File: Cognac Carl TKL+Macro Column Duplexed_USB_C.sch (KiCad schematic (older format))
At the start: 202 parts, among them SW1 SW_Push, U1 ATmega32U4-AU, Y1 16MHz

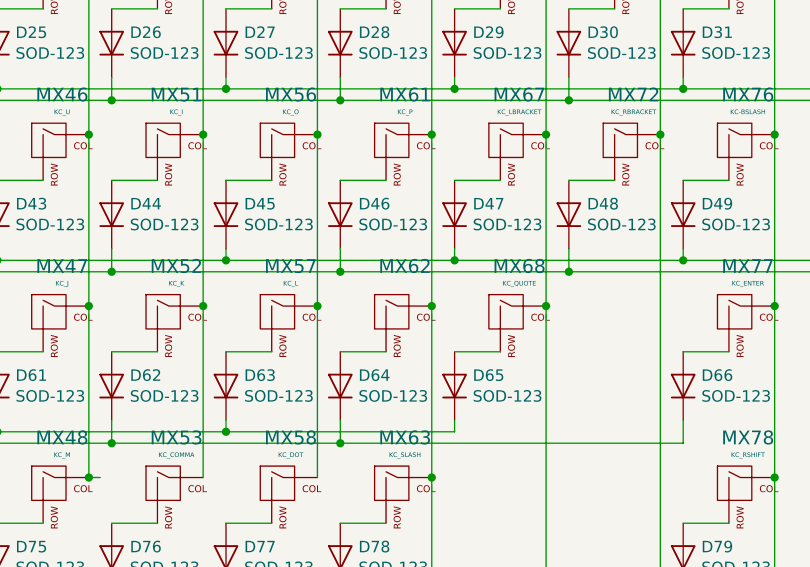
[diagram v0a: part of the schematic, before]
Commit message: Ran column traces, debating on whether to have columns on front or back of pcb
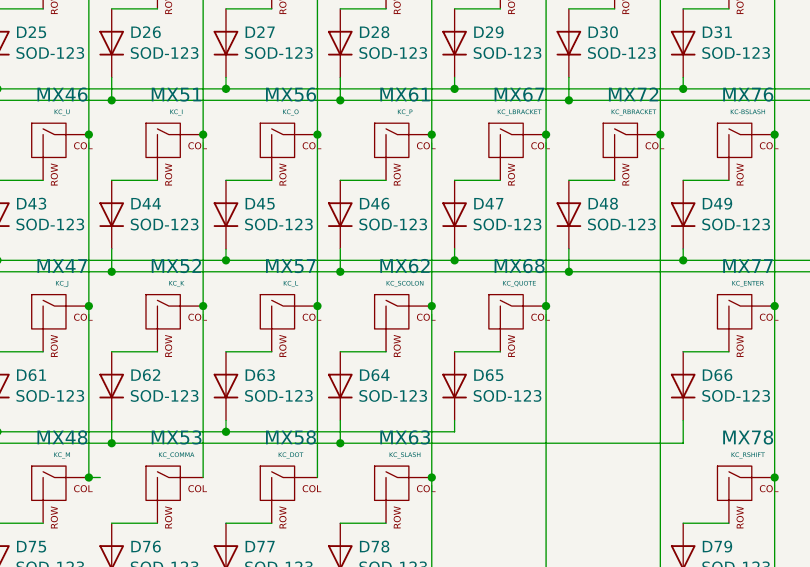
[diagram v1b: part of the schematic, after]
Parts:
- MX62: value (none) -> KC_SCOLON
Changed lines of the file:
@@
 P 7850 4050
 F 0 "MX62" H 7883 4273 60  0000 C CNN
-F 1 "KC_SCOLON
-" H 7883 4199 20  0000 C CNN
+F 1 "KC_SCOLON" H 7883 4199 20  0000 C CNN
 F 2 "MX_Only:MXOnly-1U-Hotswap" H 7225 4025 60  0001 C CNN
 F 3 "" H 7225 4025 60  0001 C CNN

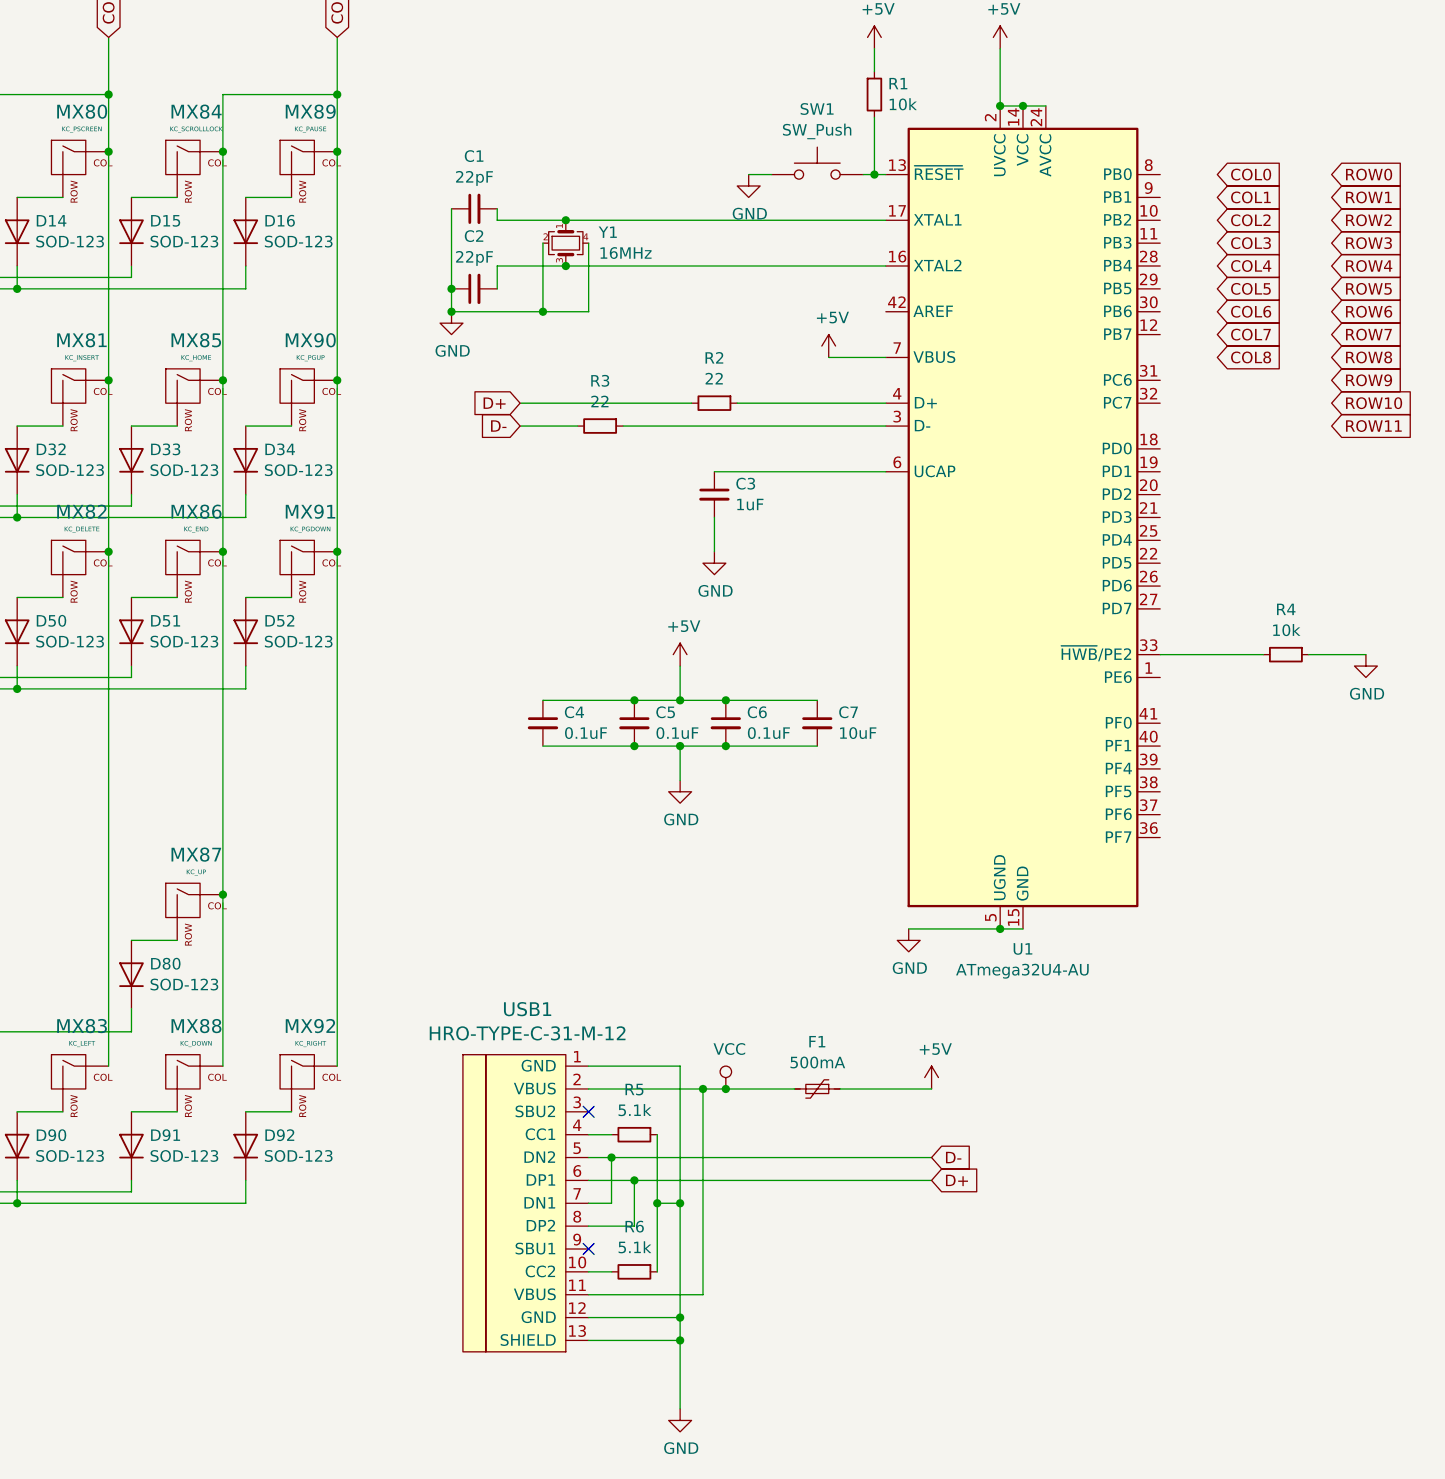
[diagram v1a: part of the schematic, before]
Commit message: completed routing, removed hotswap, added esd protection
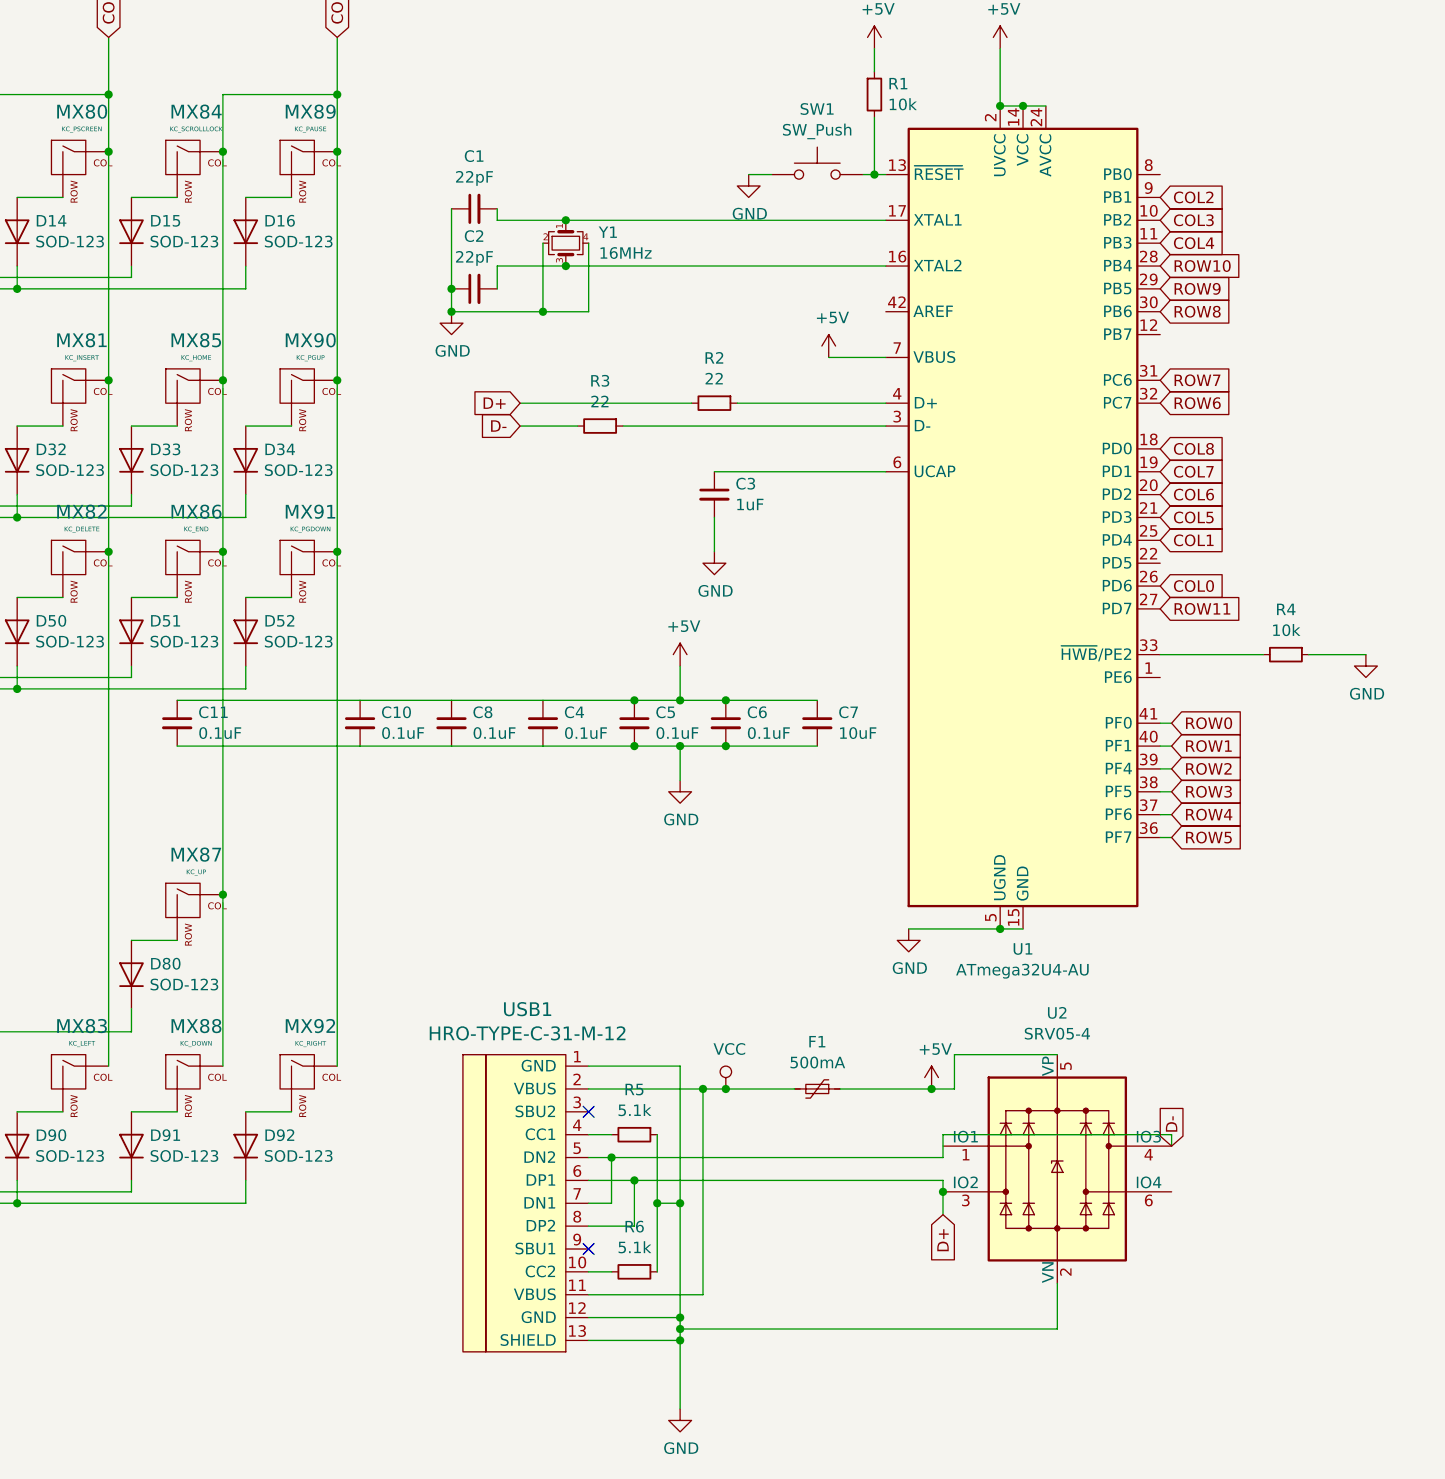
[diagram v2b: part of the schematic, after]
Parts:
- added C10, C11, C8: 0.1uF, Capacitor_SMD:C_0805_2012Metric, symbol Device:C_Small
- added U2: SRV05-4, Package_TO_SOT_SMD:SOT-23-6, symbol Power_Protection:SRV05-4
- MX1, MX12, MX13, MX14, MX15, MX17, MX18, MX19, MX2, MX20, MX21, MX23, MX24, MX25, MX26, MX27, MX28, MX29, MX3, MX30, MX31, MX32, MX33, MX34, MX35, MX36, MX37, MX38, MX39, MX4, MX40, MX41, MX42, MX44, MX45, MX46, MX47, MX48, MX49, MX5, MX50, MX51, MX52, MX53, MX54, MX55, MX56, MX57, MX58, MX59, MX6, MX60, MX61, MX62, MX63, MX65, MX66, MX67, MX68, MX7, MX70, MX71, MX72, MX74, MX80, MX81, MX82, MX83, MX84, MX85, MX86, MX87, MX88, MX89, MX90, MX91, MX92: footprint MX_Only:MXOnly-1U-Hotswap -> MX_Only:MXOnly-1U-NoLED
- MX10, MX77: footprint MX_Only:MXOnly-2.25U-Hotswap -> MX_Only:MXOnly-2.25U-NoLED
- MX11, MX16, MX22, MX64, MX69, MX73, MX79: footprint MX_Only:MXOnly-1.25U-Hotswap -> MX_Only:MXOnly-1.25U-NoLED
- MX43: footprint MX_Only:MXOnly-6.25U-Hotswap-ReversedStabilizers -> MX_Only:MXOnly-6.25U-ReversedStabilizers-NoLED
- MX75: footprint MX_Only:MXOnly-2U-Hotswap -> MX_Only:MXOnly-2U-NoLED
- MX76, MX8: footprint MX_Only:MXOnly-1.5U-Hotswap -> MX_Only:MXOnly-1.5U-NoLED
- MX78: footprint MX_Only:MXOnly-2.75U-Hotswap -> MX_Only:MXOnly-2.75U-NoLED
- MX9: footprint MX_Only:MXOnly-1.75U-Hotswap -> MX_Only:MXOnly-1.75U-NoLED
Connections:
- net +5V: now also C10.1, C11.1, C8.1, U2.5 (VP)
- net COL0: now also U1.26 (PD6)
- net COL1: now also U1.25 (PD4)
- net COL2: now also U1.9 (PB1)
- net COL3: now also U1.10 (PB2)
- net COL4: now also U1.11 (PB3)
- net COL5: now also U1.21 (PD3)
- net COL6: now also U1.20 (PD2)
- net COL7: now also U1.19 (PD1)
- net COL8: now also U1.18 (PD0)
- net D+: now also U2.3 (IO2)
- net D-: now also U2.4 (IO3)
- net GND: now also C10.2, C11.2, C8.2, U2.2 (VN)
- net ROW0: now also U1.41 (PF0)
- net ROW1: now also U1.40 (PF1)
- net ROW10: now also U1.28 (PB4)
- net ROW11: now also U1.27 (PD7)
- net ROW2: now also U1.39 (PF4)
- net ROW3: now also U1.38 (PF5)
- net ROW4: now also U1.37 (PF6)
- net ROW5: now also U1.36 (PF7)
- net ROW6: now also U1.32 (PC7)
- net ROW7: now also U1.31 (PC6)
- net ROW8: now also U1.30 (PB6)
- net ROW9: now also U1.29 (PB5)

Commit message: replaced crytsal with a murata oscillator. tidied up routing, and added filled zones.
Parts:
- removed C1, C2: 22pF, Capacitor_SMD:C_0805_2012Metric, symbol Device:C_Small
- removed Y1: 16MHz, Crystal:Crystal_SMD_3225-4Pin_3.2x2.5mm, symbol Device:Crystal_GND24_Small
- added D93, D94, D95: LED, LED_SMD:LED_0805_2012Metric, symbol Device:LED
- added R7, R8, R9: R_Small, Resistor_SMD:R_0805_2012Metric, symbol Device:R_Small
- added Y1: 16MHz, Crystal:Resonator_SMD_muRata_CSTxExxV-3Pin_3.0x1.1mm, symbol Device:Crystal_GND2_Small
- MX77: footprint MX_Only:MXOnly-2.25U-NoLED -> MX_Only:MXOnly-2.25U-ReversedStabilizers-NoLED
- renumbered C11 to C1, C10 to C2, C8 to C3, C3 to C6, C6 to C7, C7 to C8, D17 to D1, D68 to D10, D82 to D11, D19 to D12, D37 to D13, D55 to D14, D69 to D15, D83 to D16, D2 to D17, D20 to D18, D38 to D19, D35 to D2, D56 to D20, D70 to D21, D84 to D22, D3 to D23, D21 to D24, D39 to D25, D57 to D26, D71 to D27, D4 to D28, D22 to D29, D53 to D3, D40 to D30, D58 to D31, D72 to D32, D5 to D33, D23 to D34, D41 to D35, D59 to D36, D73 to D37, D6 to D38, D24 to D39, D67 to D4, D42 to D40, D60 to D41, D74 to D42, D85 to D43, D7 to D44, D25 to D45, D43 to D46, D61 to D47, D75 to D48, D8 to D49, D81 to D5, D26 to D50, D44 to D51, D62 to D52, D76 to D53, D9 to D54, D27 to D55, D45 to D56, D63 to D57, D77 to D58, D10 to D59, D1 to D6, D28 to D60, D46 to D61, D64 to D62, D78 to D63, D86 to D64, D11 to D65, D29 to D66, D47 to D67, D65 to D68, D87 to D69, D18 to D7, D12 to D70, D30 to D71, D48 to D72, D88 to D73, D13 to D74, D31 to D75, D49 to D76, D66 to D77, D79 to D78, D89 to D79, D36 to D8, D14 to D80, D32 to D81, D50 to D82, D90 to D83, D15 to D84, D33 to D85, D51 to D86, D80 to D87, D91 to D88, D16 to D89, D54 to D9, D34 to D90, D52 to D91, R3 to R1, R5 to R2, R6 to R3, R2 to R4, R1 to R5, R4 to R6
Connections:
- net +5V: now also D93.2 (A), D94.2 (A), D95.2 (A)
- net COL0: now also U1.29 (PB5); no longer U1.26 (PD6)
- net COL1: now also U1.22 (PD5); no longer U1.25 (PD4)
- net COL5: now also U1.32 (PC7); no longer U1.21 (PD3)
- net COL6: now also U1.21 (PD3); no longer U1.20 (PD2)
- net COL7: now also U1.20 (PD2); no longer U1.19 (PD1)
- net COL8: now also U1.19 (PD1); no longer U1.18 (PD0)
- net GND: now also Y1.2
- net ROW10: now also U1.26 (PD6); no longer U1.28 (PB4)
- net ROW11: now also U1.25 (PD4); no longer U1.27 (PD7)
- net ROW6: now also U1.31 (PC6); no longer U1.32 (PC7)
- net ROW7: now also U1.30 (PB6); no longer U1.31 (PC6)
- net ROW8: now also U1.28 (PB4); no longer U1.30 (PB6)
- net ROW9: now also U1.27 (PD7); no longer U1.29 (PB5)
- net at U1.1 (PE6): now also R9.2
- net at U1.12 (PB7): now also R8.2
- net XTAL2: now reaches U1.16 (XTAL2)
- net XTAL2: now also Y1.3
- net XTAL1: now reaches U1.17 (XTAL1)
- net XTAL1: now also Y1.1
- net at U1.8 (PB0): now also R7.2
- new net: D93.1 (K), R7.1
- new net: D94.1 (K), R8.1
- new net: D95.1 (K), R9.1
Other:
- moved on the sheet: C1
